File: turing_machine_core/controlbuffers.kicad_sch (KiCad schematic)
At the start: 8 parts, among them U15 74LS245, U16 74LS245, U17 74LS245, U18 74LS245, U19 74LS245

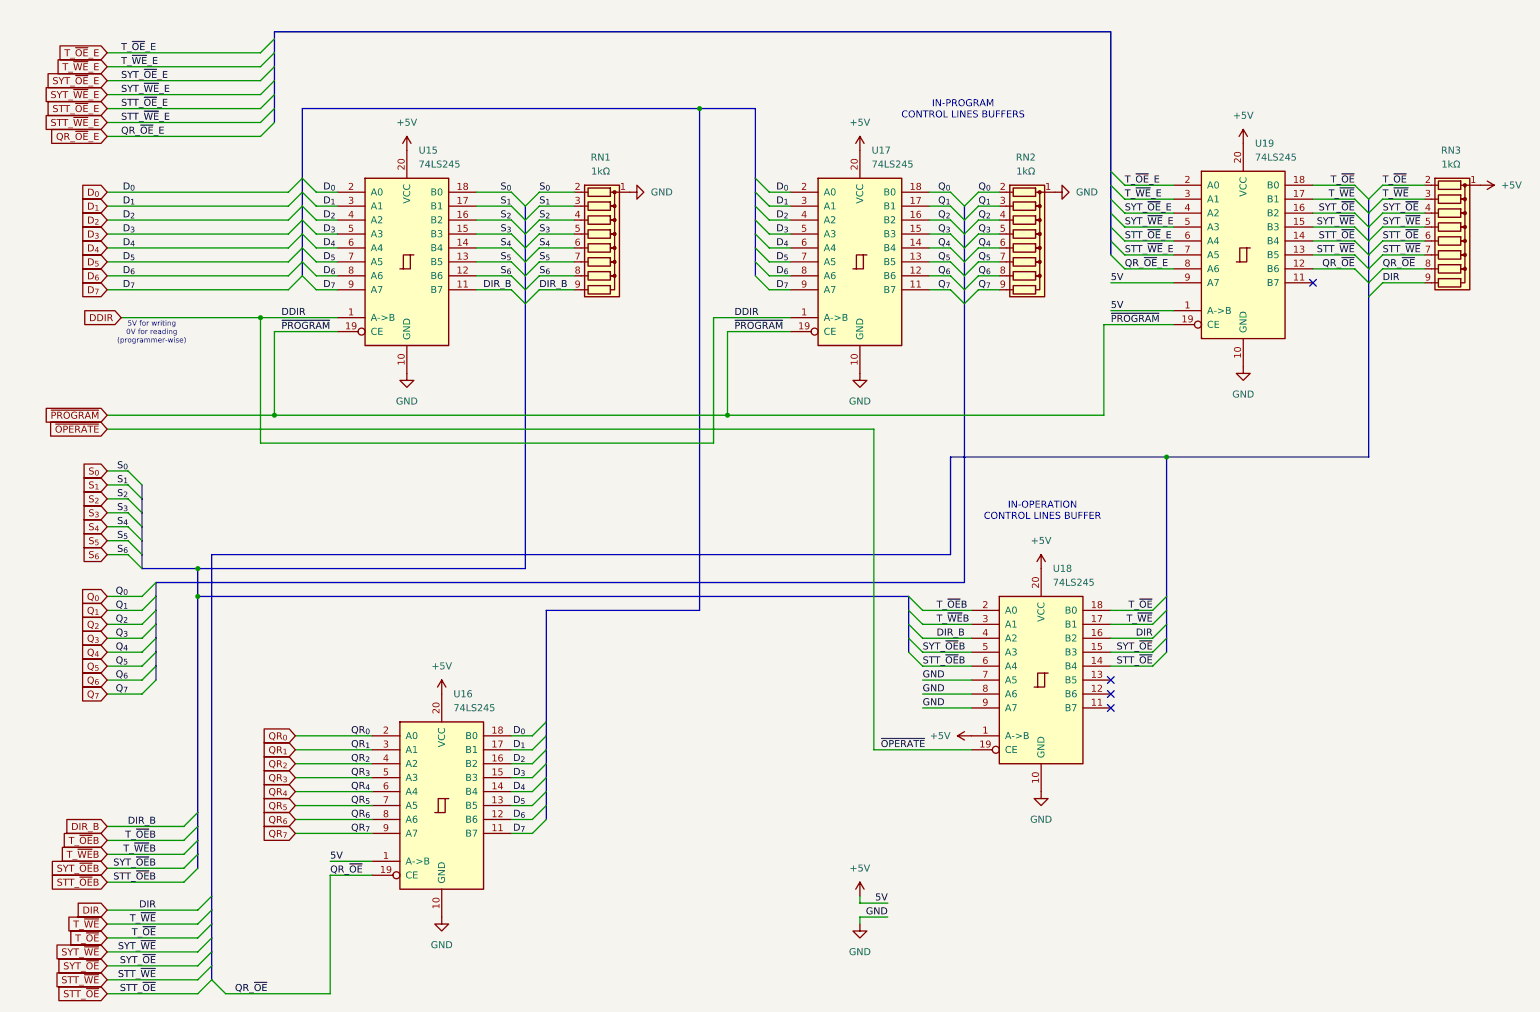
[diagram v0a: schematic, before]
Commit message: PCB layout planning and further documantation work
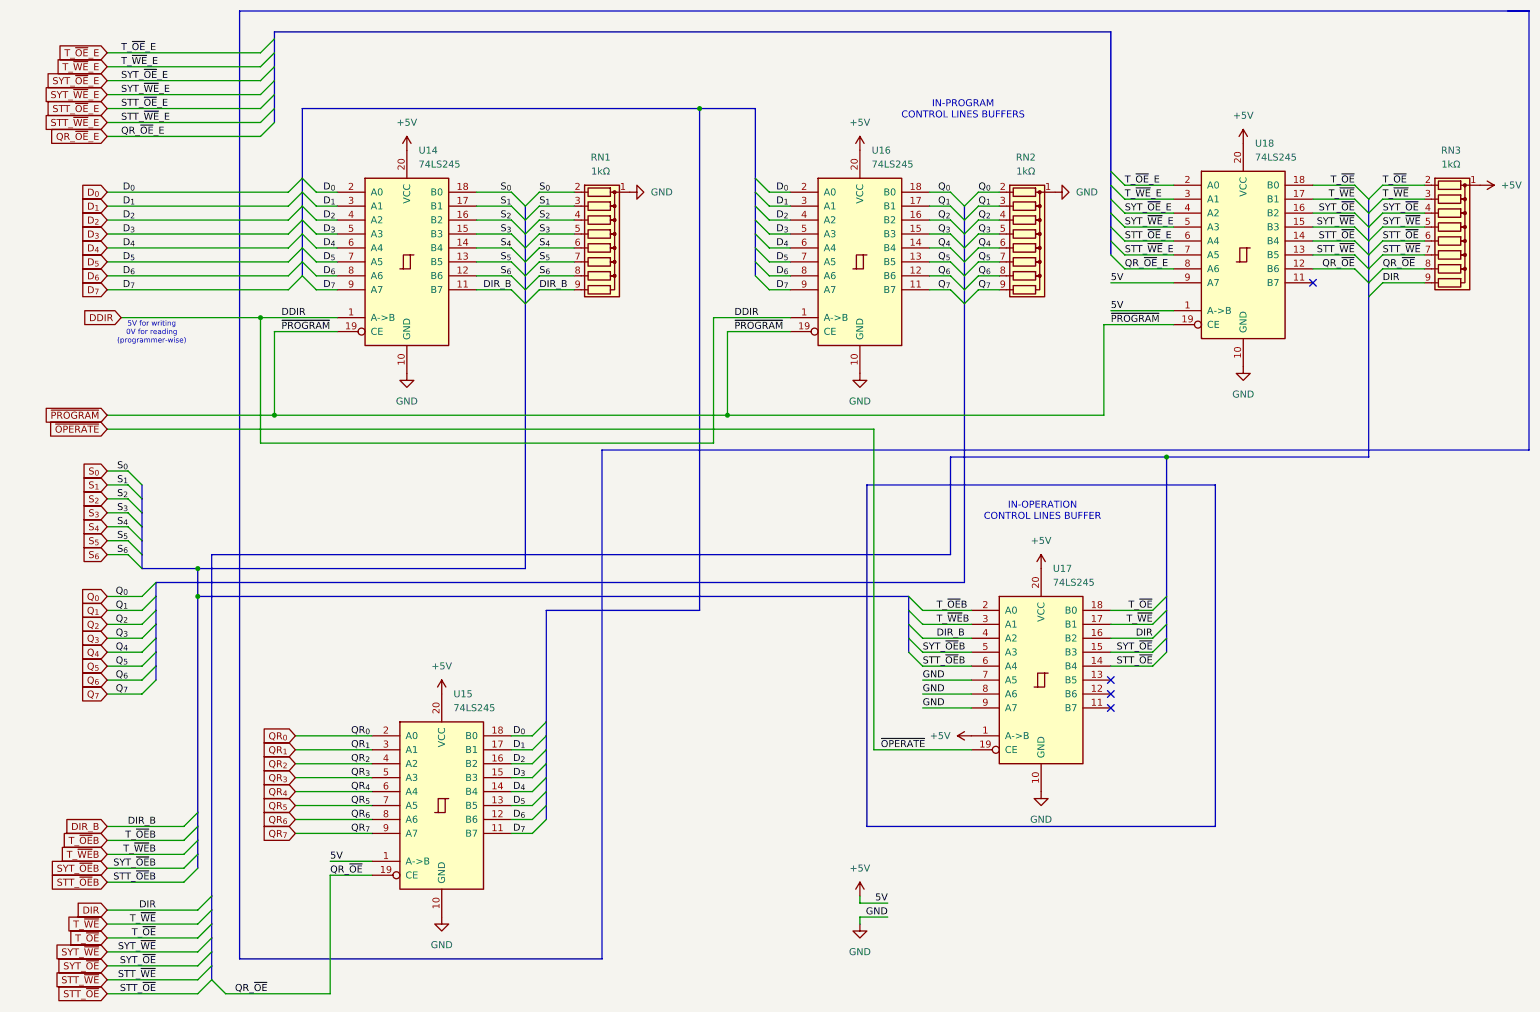
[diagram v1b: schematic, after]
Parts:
- renumbered U15 to U14, U16 to U15, U17 to U16, U18 to U17, U19 to U18
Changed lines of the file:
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@@
 	(generator_version "9.0")
 	(paper "A4")
+	(rectangle
+		(start 163.83 101.6)
+		(end 227.33 163.83)
+		(stroke
+			(width 0)
+			(type solid)
+			(color 132 132 0 1)
+		)
+		(fill
+			(type none)
+		)
+	)
 	(text "IN-OPERATION\nCONTROL LINES BUFFER"
 		(exclude_from_sim no)
@@
 		)
 	)
+	(polyline
+		(pts
+			(xy 280.67 15.24) (xy 284.48 15.24)
+		)
+		(stroke
+			(width 0)
+			(type default)
+		)
+	)
 	(bus
 		(pts
@@
 		)
 	)
+	(polyline
+		(pts
+			(xy 284.48 15.24) (xy 284.48 95.25)
+		)
+		(stroke
+			(width 0)
+			(type solid)
+			(color 132 132 0 1)
+		)
+	)
 	(wire
 		(pts
@@
 		)
 	)
+	(polyline
+		(pts
+			(xy 115.57 187.96) (xy 49.53 187.96)
+		)
+		(stroke
+			(width 0)
+			(type solid)
+			(color 132 132 0 1)
+		)
+	)
 	(wire
 		(pts
@@
 		)
 	)
+	(polyline
+		(pts
+			(xy 115.57 95.25) (xy 115.57 187.96)
+		)
+		(stroke
+			(width 0)
+			(type solid)
+			(color 132 132 0 1)
+		)
+	)
 	(bus
 		(pts
@@
 		)
 	)
+	(polyline
+		(pts
+			(xy 49.53 15.24) (xy 284.48 15.24)
+		)
+		(stroke
+			(width 0)
+			(type solid)
+			(color 132 132 0 1)
+		)
+	)
 	(wire
 		(pts
@@
 		)
 	)
+	(polyline
+		(pts
+			(xy 284.48 15.24) (xy 284.48 15.24)
+		)
+		(stroke
+			(width 0)
+			(type default)
+		)
+	)
 	(wire
 		(pts
@@
 		)
 	)
+	(polyline
+		(pts
+			(xy 49.53 187.96) (xy 49.53 15.24)
+		)
+		(stroke
+			(width 0)
+			(type solid)
+			(color 132 132 0 1)
+		)
+	)
 	(wire
 		(pts
@@
 		)
 	)
+	(polyline
+		(pts
+			(xy 284.48 95.25) (xy 115.57 95.25)
+		)
+		(stroke
+			(width 0)
+			(type solid)
+			(color 132 132 0 1)
+		)
+	)
 	(wire
 		(pts
@@
 		(dnp no)
 		(fields_autoplaced yes)
-		(property "Reference" "U18"
+		(property "Reference" "U17"
 			(at 197.7233 116.84 0)
 			(effects
@@
 			(project "turing_machine"
 				(path "/c2889866-f59b-4a7d-9ec7-f6fbf53024cb/95b00103-b1d8-417f-a672-0089eab2b908"
-					(reference "U18")
+					(reference "U17")
 					(unit 1)
 				)
@@
 		(dnp no)
 		(fields_autoplaced yes)
-		(property "Reference" "U15"
+		(property "Reference" "U14"
 			(at 82.1533 40.64 0)
 			(effects
@@
 			(project "turing_machine"
 				(path "/c2889866-f59b-4a7d-9ec7-f6fbf53024cb/95b00103-b1d8-417f-a672-0089eab2b908"
-					(reference "U15")
+					(reference "U14")
 					(unit 1)
 				)
@@
 		(dnp no)
 		(fields_autoplaced yes)
-		(property "Reference" "U16"
+		(property "Reference" "U15"
 			(at 88.5033 139.7 0)
 			(effects
@@
 			(project "turing_machine"
 				(path "/c2889866-f59b-4a7d-9ec7-f6fbf53024cb/95b00103-b1d8-417f-a672-0089eab2b908"
-					(reference "U16")
+					(reference "U15")
 					(unit 1)
 				)
@@
 		(dnp no)
 		(fields_autoplaced yes)
-		(property "Reference" "U19"
+		(property "Reference" "U18"
 			(at 234.5533 39.37 0)
 			(effects
@@
 			(project "turing_machine"
 				(path "/c2889866-f59b-4a7d-9ec7-f6fbf53024cb/95b00103-b1d8-417f-a672-0089eab2b908"
-					(reference "U19")
+					(reference "U18")
 					(unit 1)
 				)
@@
 		(dnp no)
 		(fields_autoplaced yes)
-		(property "Reference" "U17"
+		(property "Reference" "U16"
 			(at 164.7033 40.64 0)
 			(effects
@@
 			(project "turing_machine"
 				(path "/c2889866-f59b-4a7d-9ec7-f6fbf53024cb/95b00103-b1d8-417f-a672-0089eab2b908"
-					(reference "U17")
+					(reference "U16")
 					(unit 1)
 				)

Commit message: fixed schematics bugs and updated documentation
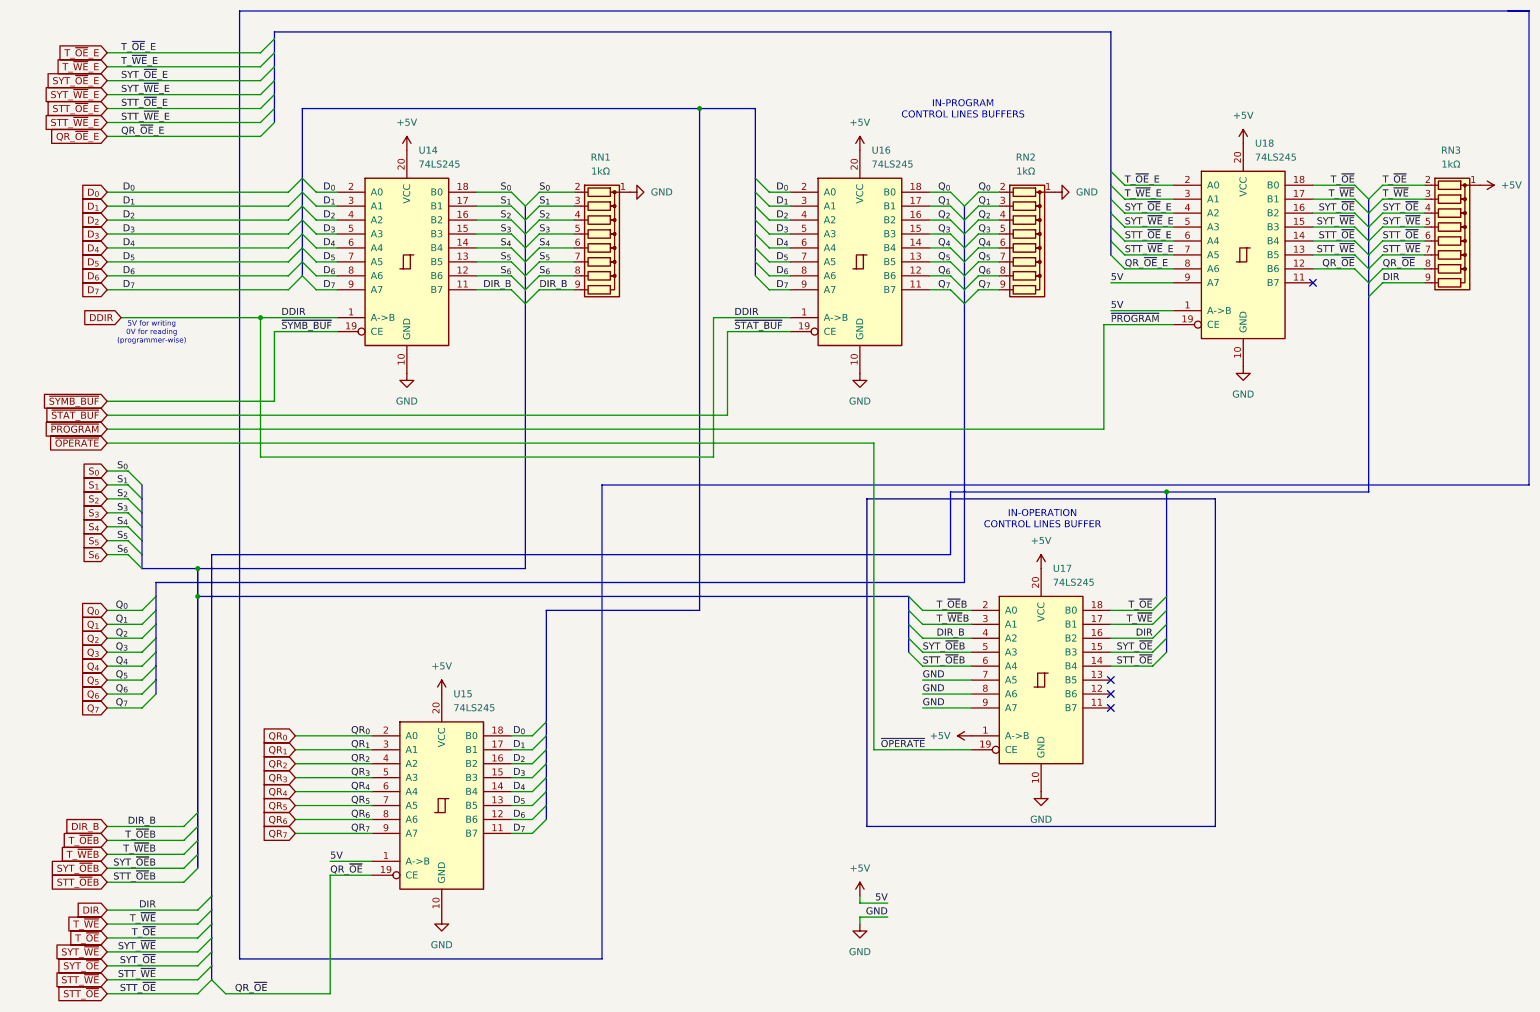
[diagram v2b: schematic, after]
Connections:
- net ~{PROGRAM}: no longer U14.19 (CE), U16.19 (CE)
- new net ~{STAT_BUF}: U16.19 (CE)
- new net ~{SYMB_BUF}: U14.19 (CE)
